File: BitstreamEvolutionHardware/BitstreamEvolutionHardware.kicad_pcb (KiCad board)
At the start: 2 copper layers, 98.9 x 97 mm, 89 parts, among them J1 CONN10_N-RC_SUL, J10 61300211121, J11 61300211121, J12 61300211121, J13 61300211121, J14 61300211121, J15 61300211121, J16 61300211121, J17 61300211121, J18 61300211121, J19 61300211121, J2 CONN10_N-RC_SUL, J20 61300211121, J21 61300211121, J22 61300211121, J23 61300211121, J24 61300211121, J25 61300211121, J26 61300211121, J27 61300211121, J28 61300211121, J29 61300211121, J3 61300211121, J30 61300211121, J31 61300211121, J32 61300211121, J33 61300211121, J34 61300211121, J35 61300211121, J36 61300211121, J37 61300211121, J38 61300211121, J39 61300211121, J4 61300211121, J40 61300211121, J41 61300211121, J42 61300211121, J43 61300211121, J44 61300211121, J45 61300211121, J5 61300211121, J6 61300211121, J7 61300211121, J8 61300211121, J9 61300211121, Q1 BSS138, Q2 BSS138, U1 ADS7828, U2 ADS7828, U3 PPTC151LFBN-RC, U4 PPTC151LFBN-RC, U5 MCP4728, U7 RT9193-33GB, U8 Si5351A-B-GT, Y1 ABM8G-25.000MHZ-4Y-T3

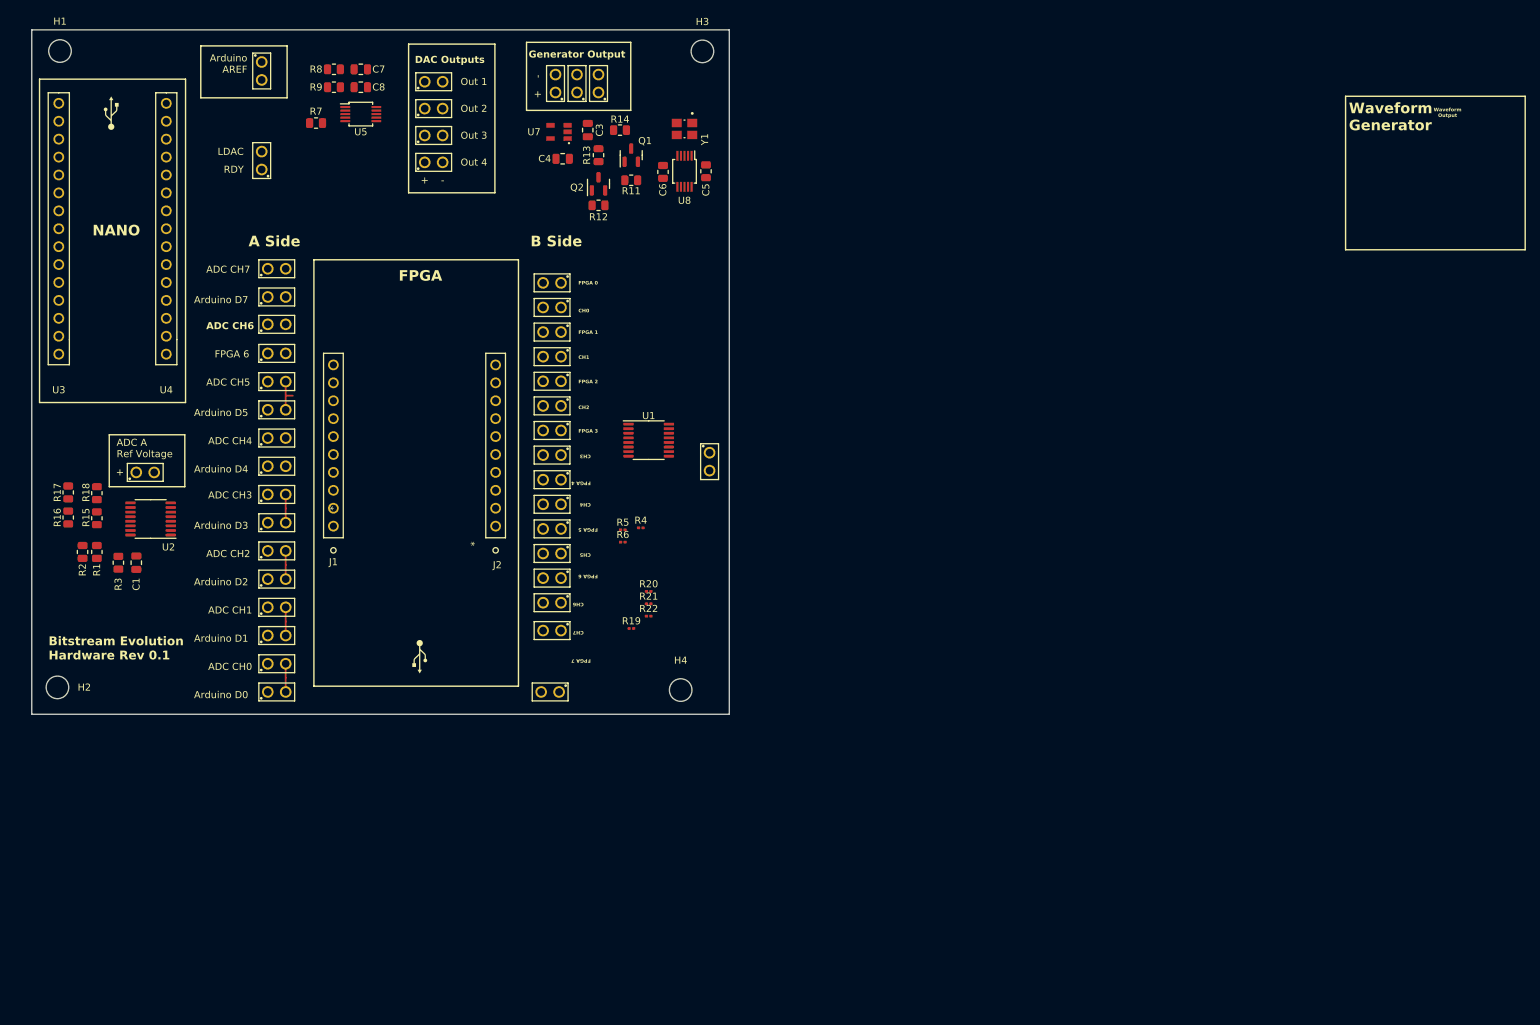
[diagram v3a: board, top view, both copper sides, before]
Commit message: Almost Done with Routing, need to route power and I2C Lines
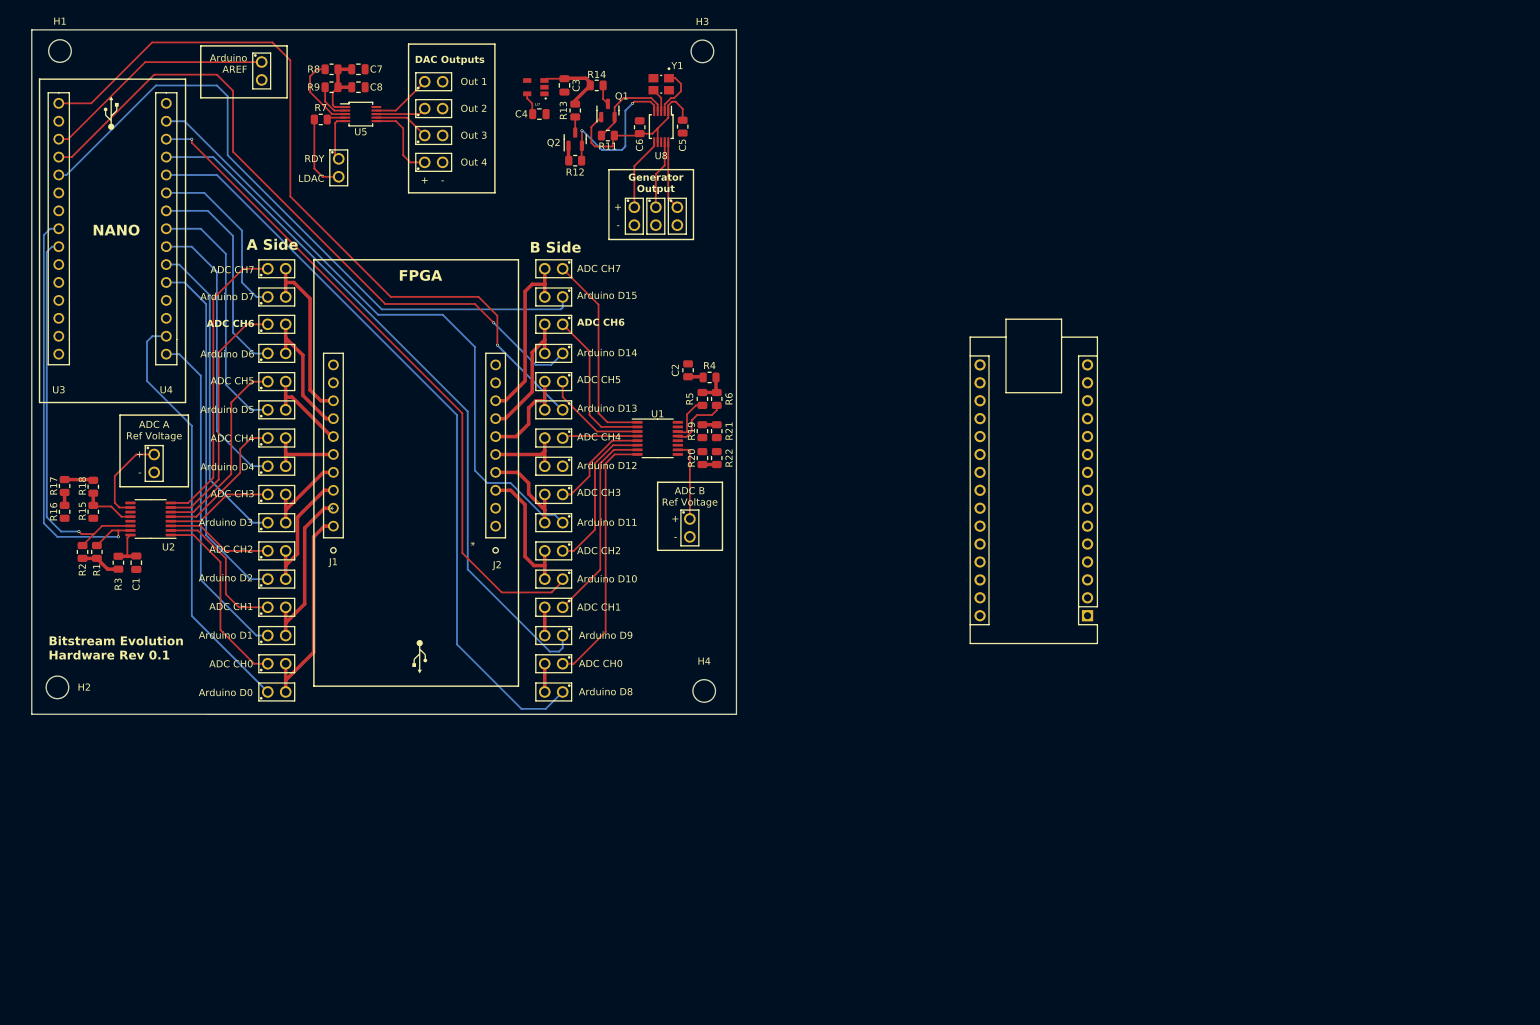
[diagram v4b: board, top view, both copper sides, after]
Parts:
- added A1: Arduino_Nano_Every, Module:Arduino_Nano, F.Cu at (186.7, 99.1)
- added C2: 10uF, Resistor_SMD:R_0805_2012Metric, F.Cu at (130.0, 64.3)
- J1, J2: value CONN10_N-RC_SUL -> PPPC101LFBN-RC
- R19, R20, R21, R22, R4, R5, R6: footprint Resistor_SMD:R_0201_0603Metric -> Resistor_SMD:R_0805_2012Metric
- moved R19 29.7 mm to (132.1, 72.9), turned to -90 degrees
- moved R21 26.3 mm to (134.1, 72.9), turned to -90 degrees
- moved J38 25.5 mm to (128.5, 42.4), turned to -90 degrees
- moved R22 24.4 mm to (134.1, 76.7), turned to -90 degrees
- moved R6 24.3 mm to (134.1, 68.3), turned to -90 degrees
- moved R4 23.4 mm to (133.1, 65.3)
- moved J41 21.9 mm to (125.5, 42.4), turned to -90 degrees
- moved R5 21.7 mm to (132.1, 68.3), turned to -90 degrees
- moved R20 20.4 mm to (132.1, 76.7), turned to -90 degrees
- moved J40 19.5 mm to (122.4, 42.4), turned to -90 degrees
- moved J44 11.0 mm to (80.5, 35.6), turned to -90 degrees
- moved J39 9.80 mm to (130.3, 86.6)
- moved R11 7.14 mm to (118.7, 31.0)
- moved C4 7.14 mm to (109.0, 27.9)
- moved C6 7.14 mm to (123.2, 29.8)
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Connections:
- J1 pad 9: unconnected-(J1-Pad9) -> GND
- J2 pad 9: unconnected-(J2-Pad9) -> GND
- R20 pad 1: Net-(U1-A1) -> Net-(U1-A0)
- R21 pad 2: Net-(U1-A0) -> Net-(U1-A1)
- R22 pad 1: Net-(U1-A0) -> Net-(U1-A1)
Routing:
- net /Arduino_D13: track 0.00 -> 110.3 mm, vias 0 -> 1
- net /Arduino_D8: track 0.00 -> 107.6 mm
- net /Arduino_D9: track 0.00 -> 100.3 mm
- net /Arduino_D14: track 0.00 -> 99.1 mm, vias 0 -> 1
- net /Arduino_D15: track 0.00 -> 96.4 mm
- net /Arduino_D10: track 0.00 -> 95.7 mm, vias 0 -> 1
- net /Arduino_D11: track 0.00 -> 90.0 mm
- net /Arduino_SCL: track 0.00 -> 77.9 mm, vias 0 -> 1
- net /Arduino_SDA: track 0.00 -> 75.4 mm, vias 0 -> 1
- net /Arduino_D0: track 0.00 -> 59.8 mm
- net /Arduino_D2: track 0.00 -> 51.0 mm
- net /Arduino_D1: track 0.10 -> 48.0 mm
- net /Arduino_D3: track 0.00 -> 44.9 mm
- net /ADC_A_Channel_7: track 0.00 -> 42.4 mm
- net /Arduino_D4: track 0.00 -> 40.5 mm
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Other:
- board size 98.9 x 97 mm -> 99.9 x 97 mm
- copper layers 2 -> 4
- board text added: "ADC B Ref Voltage"
- board text added: "Arduino D10"
- board text added: "Arduino D11"
- board text added: "Arduino D12"
- board text added: "Arduino D13"
- board text added: "Arduino D14"
- board text added: "Arduino D15"
- board text added: "Arduino D6"
- board text added: "Arduino D8"
- board text added: "Arduino D9"
- board text removed: "CH0"
- board text removed: "CH1"
- board text removed: "CH2"
- board text removed: "CH3"
- board text removed: "CH4"
- board text removed: "CH5"
- board text removed: "CH6"
- board text removed: "CH7"
- board text removed: "FPGA 0"
- board text removed: "FPGA 1"
- board text removed: "FPGA 2"
- board text removed: "FPGA 3"
- board text removed: "FPGA 4"
- board text removed: "FPGA 5"
- board text removed: "FPGA 6"
- board text removed: "FPGA 7"
- board text removed: "Waveform Generator"
- board text removed: "Waveform Output"
